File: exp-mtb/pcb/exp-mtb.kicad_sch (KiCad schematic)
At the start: 67 parts, among them J2 Conn_02x05, J3 ARK2500R-A-2P, J4 ARK2500R-A-2P, J5 AVR-ISP-6, Q1 BT148, SW1 SW_Push, U1 ADUM1250, U2 6N137, U3 6N137, U4 ATmega328P-AU, U5 L78L05_SOT89, U6 SN75176AD, U7 PC817, Y1 14.745 MHz

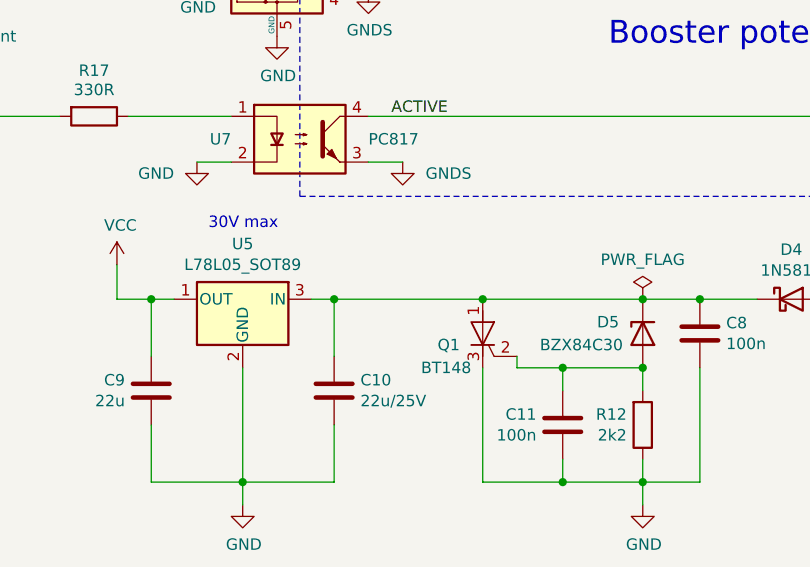
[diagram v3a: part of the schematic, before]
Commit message: exp-mtb: use 78M05 instead of 78L05.
75176 can draw quite high current.
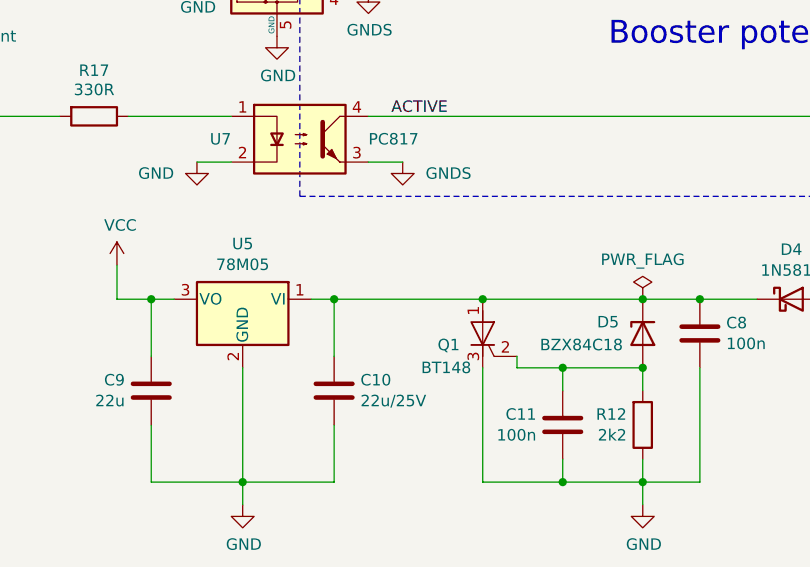
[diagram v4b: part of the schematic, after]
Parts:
- D5: value BZX84C30 -> BZX84C18
- H1, H2, H3, H4: footprint MountingHole:MountingHole_3.2mm_M3_Pad_Via -> MountingHole:MountingHole_3.2mm_M3_Pad
- SW1: footprint Button_Switch_THT:SW_PUSH_6mm -> Button_Switch_THT:SW_PUSH_6mm_H4.3mm
- TP3: footprint TestPoint:TestPoint_Loop_D3.50mm_Drill1.4mm_Beaded -> TestPoint:TestPoint_Loop_D1.80mm_Drill1.0mm_Beaded
- U5: value L78L05_SOT89 -> 78M05; footprint Package_TO_SOT_SMD:SOT-89-3 -> Package_TO_SOT_SMD:TO-252-2; symbol Regulator_Linear:L78L05_SOT89 -> Regulator_Linear:KA78M05_TO252
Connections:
- net VCC: now also U5.3 (VO); no longer U5.1 (OUT)
- net at C10.1, C8.1, D4.1 (K)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: now also U5.1 (VI); no longer U5.3 (IN)
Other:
- note removed: "30V max"
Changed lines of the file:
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@@
 		)
 	)
-	(text "30V max"
-		(exclude_from_sim no)
-		(at 170.18 128.27 0)
-		(effects
-			(font
-				(size 1.27 1.27)
-			)
-			(justify left bottom)
-		)
-	)
 	(text "Booster potential"
 		(exclude_from_sim no)
@@
 			)
 		)
-		(property "Value" "BZX84C30"
+		(property "Value" "BZX84C18"
 			(at 207.01 140.97 90)
 			(effects
@@
 			)
 		)
-		(property "Footprint" "Button_Switch_THT:SW_PUSH_6mm"
+		(property "Footprint" "Button_Switch_THT:SW_PUSH_6mm_H4.3mm"
 			(at 107.95 100.33 0)
 			(effects
@@
 	)
 	(symbol
-		(lib_id "Regulator_Linear:L78L05_SOT89")
+		(lib_id "Regulator_Linear:KA78M05_TO252")
 		(at 173.99 135.89 0)
 		(mirror y)
@@
 			)
 		)
-		(property "Value" "L78L05_SOT89"
+		(property "Value" "78M05"
 			(at 173.99 132.0546 0)
 			(effects
@@
 			)
 		)
-		(property "Footprint" "Package_TO_SOT_SMD:SOT-89-3"
-			(at 173.99 130.81 0)
+		(property "Footprint" "Package_TO_SOT_SMD:TO-252-2"
+			(at 173.99 130.175 0)
 			(effects
 				(font
@@
 			)
 		)
-		(property "Datasheet" "http://www.st.com/content/ccc/resource/technical/document/datasheet/15/55/e5/aa/23/5b/43/fd/CD00000446.pdf/files/CD00000446.pdf/jcr:content/translations/en.CD00000446.pdf"
+		(property "Datasheet" "https://www.onsemi.com/pub/Collateral/MC78M00-D.PDF"
 			(at 173.99 137.16 0)
 			(effects
@@
 			)
 		)
-		(property "Description" "Positive 100mA 30V Linear Regulator, Fixed Output 5V, SOT-89"
+		(property "Description" "Positive 500mA 35V Linear Regulator, Fixed Output 5V, TO-252 (D-PAK)"
 			(at 173.99 135.89 0)
 			(effects
@@
 			)
 		)
-		(property "Footprint" "TestPoint:TestPoint_Loop_D3.50mm_Drill1.4mm_Beaded"
+		(property "Footprint" "TestPoint:TestPoint_Loop_D1.80mm_Drill1.0mm_Beaded"
 			(at 135.89 180.34 0)
 			(effects
@@
 			)
 		)
-		(property "Footprint" "MountingHole:MountingHole_3.2mm_M3_Pad_Via"
+		(property "Footprint" "MountingHole:MountingHole_3.2mm_M3_Pad"
 			(at 157.48 177.8 0)
 			(effects
@@
 			)
 		)
-		(property "Footprint" "MountingHole:MountingHole_3.2mm_M3_Pad_Via"
+		(property "Footprint" "MountingHole:MountingHole_3.2mm_M3_Pad"
 			(at 157.48 182.88 0)
 			(effects
@@
 			)
 		)
-		(property "Footprint" "MountingHole:MountingHole_3.2mm_M3_Pad_Via"
+		(property "Footprint" "MountingHole:MountingHole_3.2mm_M3_Pad"
 			(at 162.56 177.8 0)
 			(effects
@@
 			)
 		)
-		(property "Footprint" "MountingHole:MountingHole_3.2mm_M3_Pad_Via"
+		(property "Footprint" "MountingHole:MountingHole_3.2mm_M3_Pad"
 			(at 162.56 182.88 0)
 			(effects

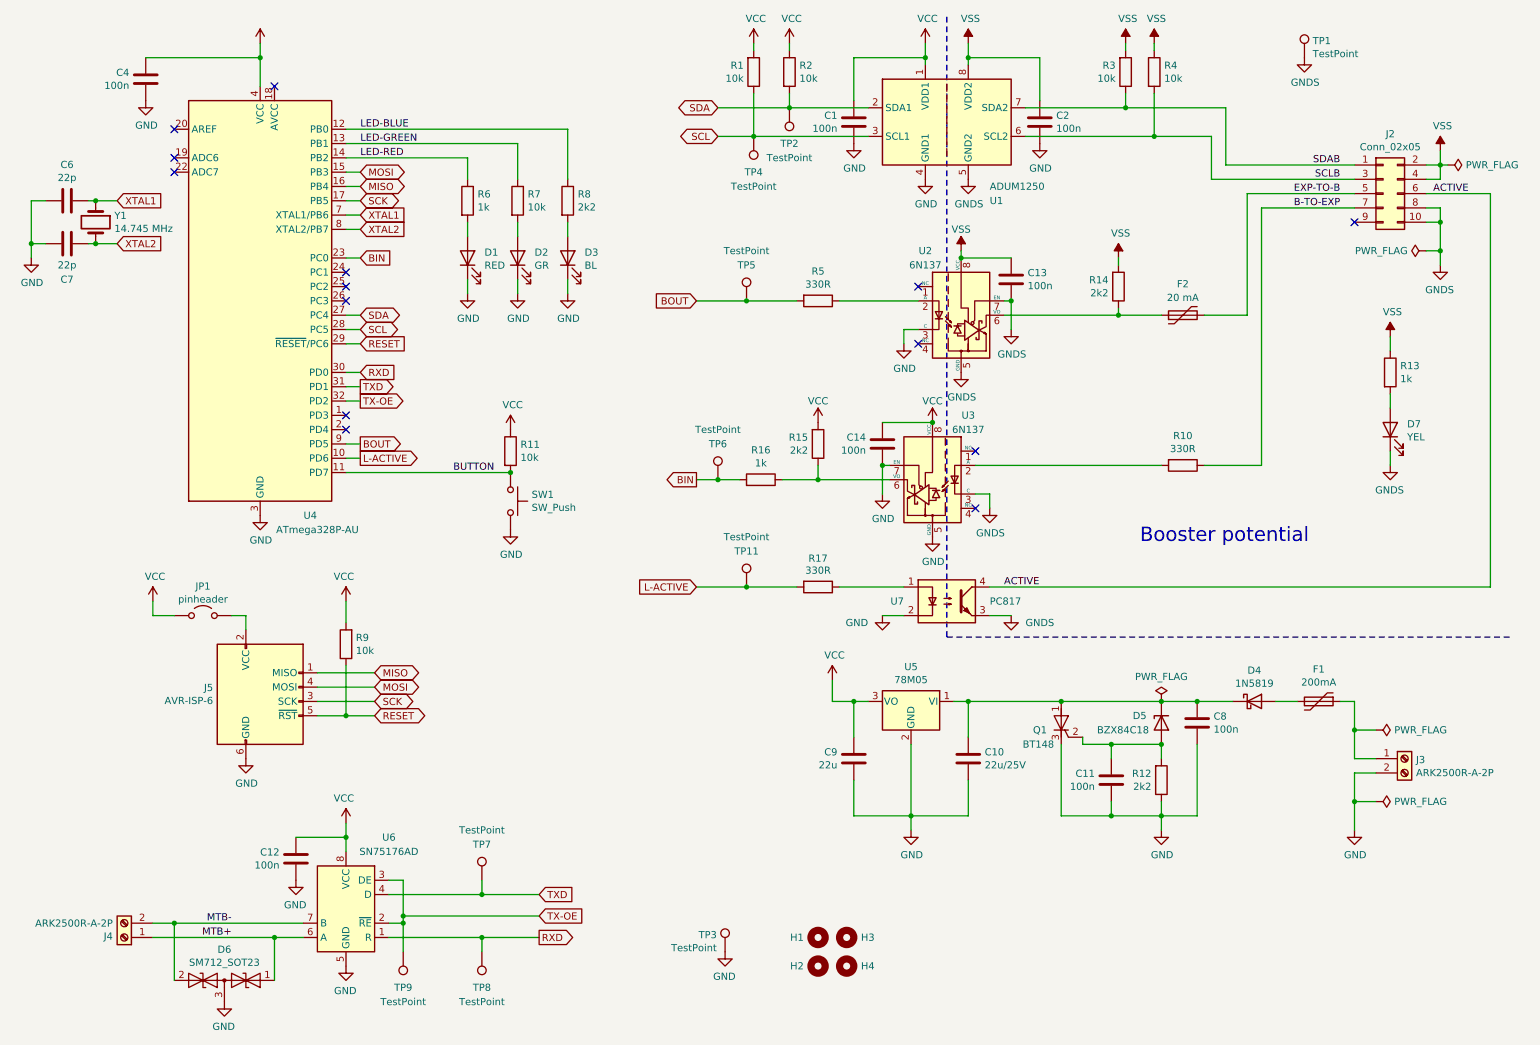
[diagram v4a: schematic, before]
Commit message: exp-mtb: use standard SMD packages, no handsolder.
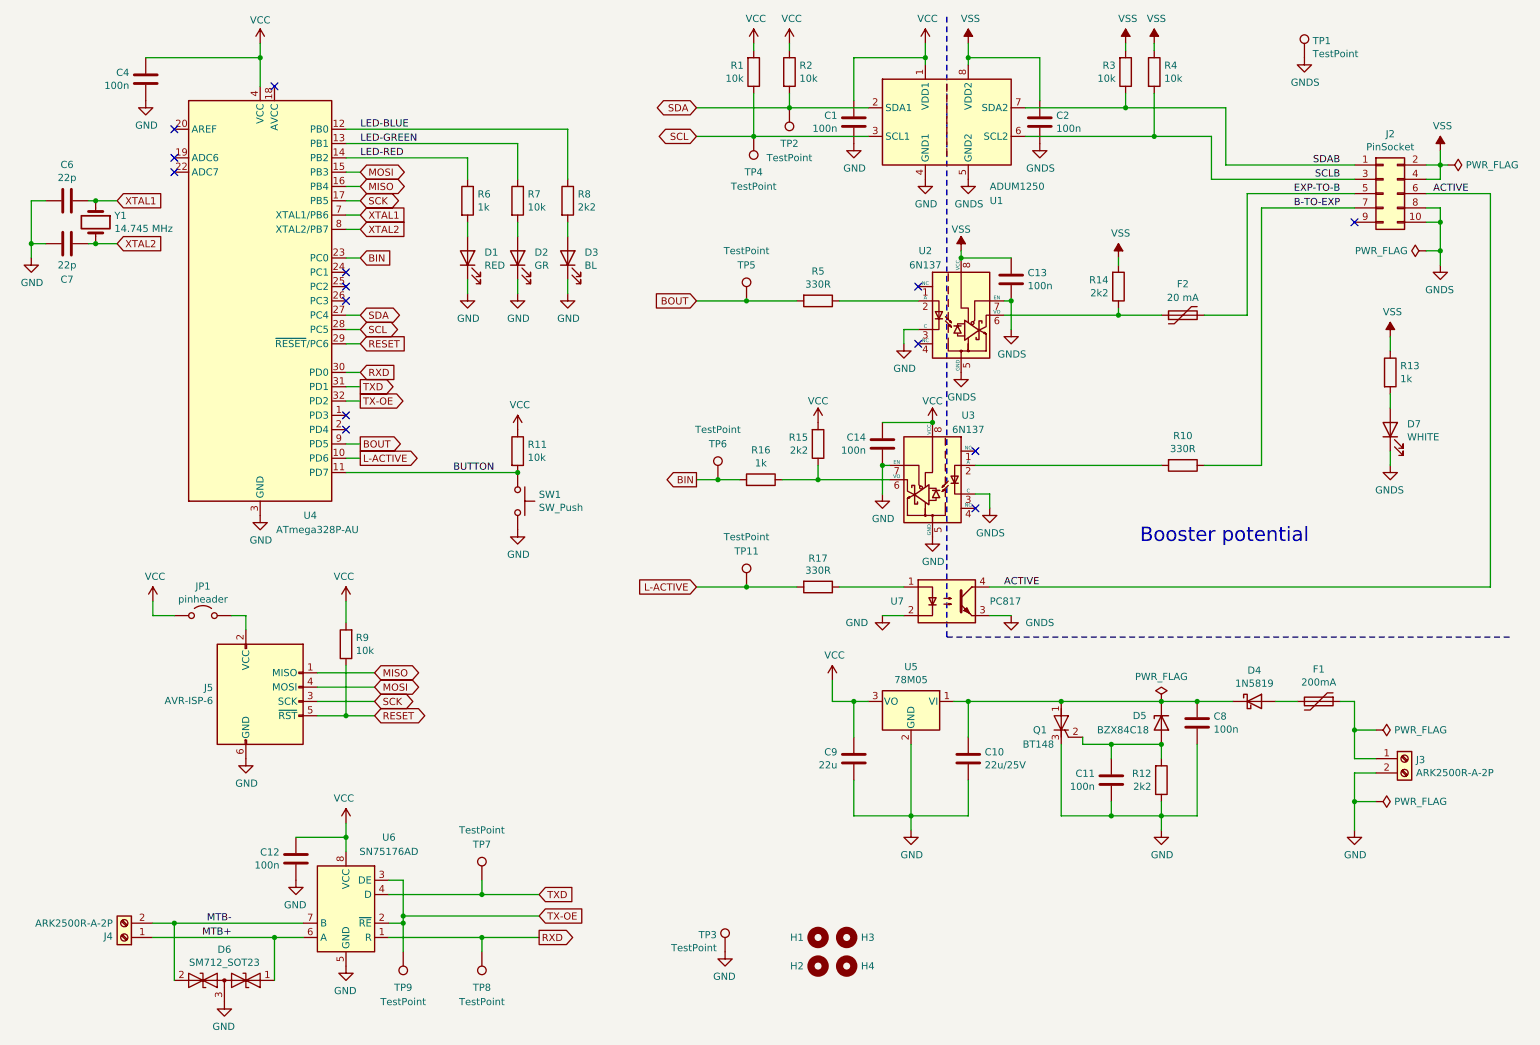
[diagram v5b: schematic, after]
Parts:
- C1, C10, C11, C12, C13, C14, C2, C4, C6, C7, C8, C9: footprint Capacitor_SMD:C_0805_2012Metric_Pad1.18x1.45mm_HandSolder -> Capacitor_SMD:C_0805_2012Metric
- D1, D2, D3: footprint LED_SMD:LED_0805_2012Metric_Pad1.15x1.40mm_HandSolder -> LED_SMD:LED_0805_2012Metric
- D7: value YEL -> WHITE; footprint LED_SMD:LED_0805_2012Metric_Pad1.15x1.40mm_HandSolder -> LED_SMD:LED_0805_2012Metric
- F1: footprint Fuse:Fuse_1206_3216Metric_Pad1.42x1.75mm_HandSolder -> Fuse:Fuse_1206_3216Metric
- J2: value Conn_02x05 -> PinSocket
- R1, R10, R11, R12, R13, R14, R15, R16, R17, R2, R3, R4, R5, R6, R7, R8, R9: footprint Resistor_SMD:R_0805_2012Metric_Pad1.20x1.40mm_HandSolder -> Resistor_SMD:R_0805_2012Metric
- TP1: footprint TestPoint:TestPoint_Loop_D3.50mm_Drill1.4mm_Beaded -> TestPoint:TestPoint_Loop_D1.80mm_Drill1.0mm_Beaded
- Y1: footprint Crystal:Crystal_SMD_HC49-SD_HandSoldering -> Crystal:Crystal_SMD_HC49-SD
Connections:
- net GND: no longer C2.2
- net GNDS: now also C2.2
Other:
- moved on the sheet: R11, SW1
